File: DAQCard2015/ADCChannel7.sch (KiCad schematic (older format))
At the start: 16 parts, among them U11 THS4524IDBTR, U12 AD9219

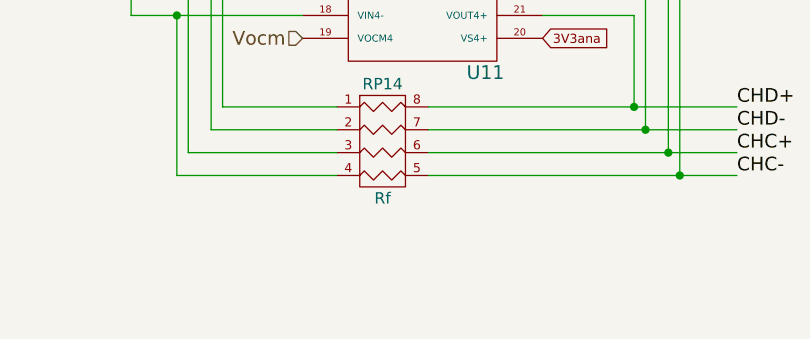
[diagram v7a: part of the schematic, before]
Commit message: Update to DAQ Board including adding an JTAG header and hooking up external clock and trigger
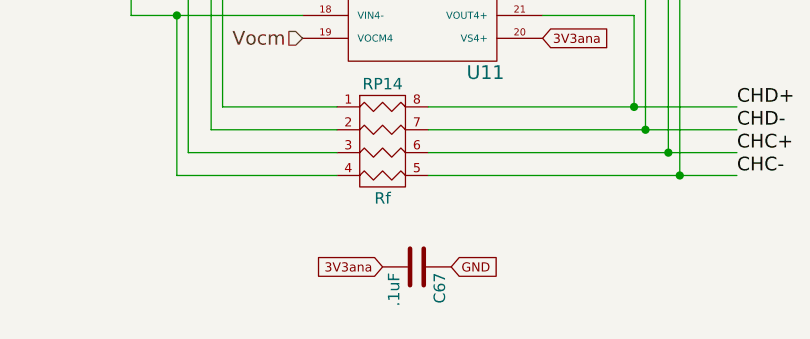
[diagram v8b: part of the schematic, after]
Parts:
- added C67: .1uF, Capacitors_SMD:C_0603, symbol C
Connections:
- net 3V3ana: now also C67.2
- net GND: now also C67.1
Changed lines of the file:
@@
 $Descr A4 11693 8268
 encoding utf-8
-Sheet 6 13
+Sheet 9 13
 Title ""
 Date ""
@@
 Text GLabel 8100 4150 0    40   Input ~ 0
 GND
+$Comp
+L C C67
+U 1 1 56064447
+P 4400 5500
+F 0 "C67" H 4425 5600 50  0000 L CNN
+F 1 ".1uF" H 4425 5400 50  0000 L CNN
+F 2 "Capacitors_SMD:C_0603" H 4438 5350 30  0001 C CNN
+F 3 "" H 4400 5500 60  0000 C CNN
+	1    4400 5500
+	0    1    1    0
+$EndComp
+Text GLabel 4250 5500 0    40   Input ~ 0
+3V3ana
+Text GLabel 4550 5500 2    40   Input ~ 0
+GND
 $EndSCHEMATC
